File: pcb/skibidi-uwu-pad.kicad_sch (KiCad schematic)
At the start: 21 parts, among them J1 Conn_01x02_Socket, SW2 RotaryEncoder_Switch, SW3 SW_Push, SW4 SW_Push, SW5 PTS526 SM15 SMTR2 LFS, U1 XIAO-nRF52840-SMD, U2 AH49FNTR-G1, U3 AH49FNTR-G1, U4 AH49FNTR-G1

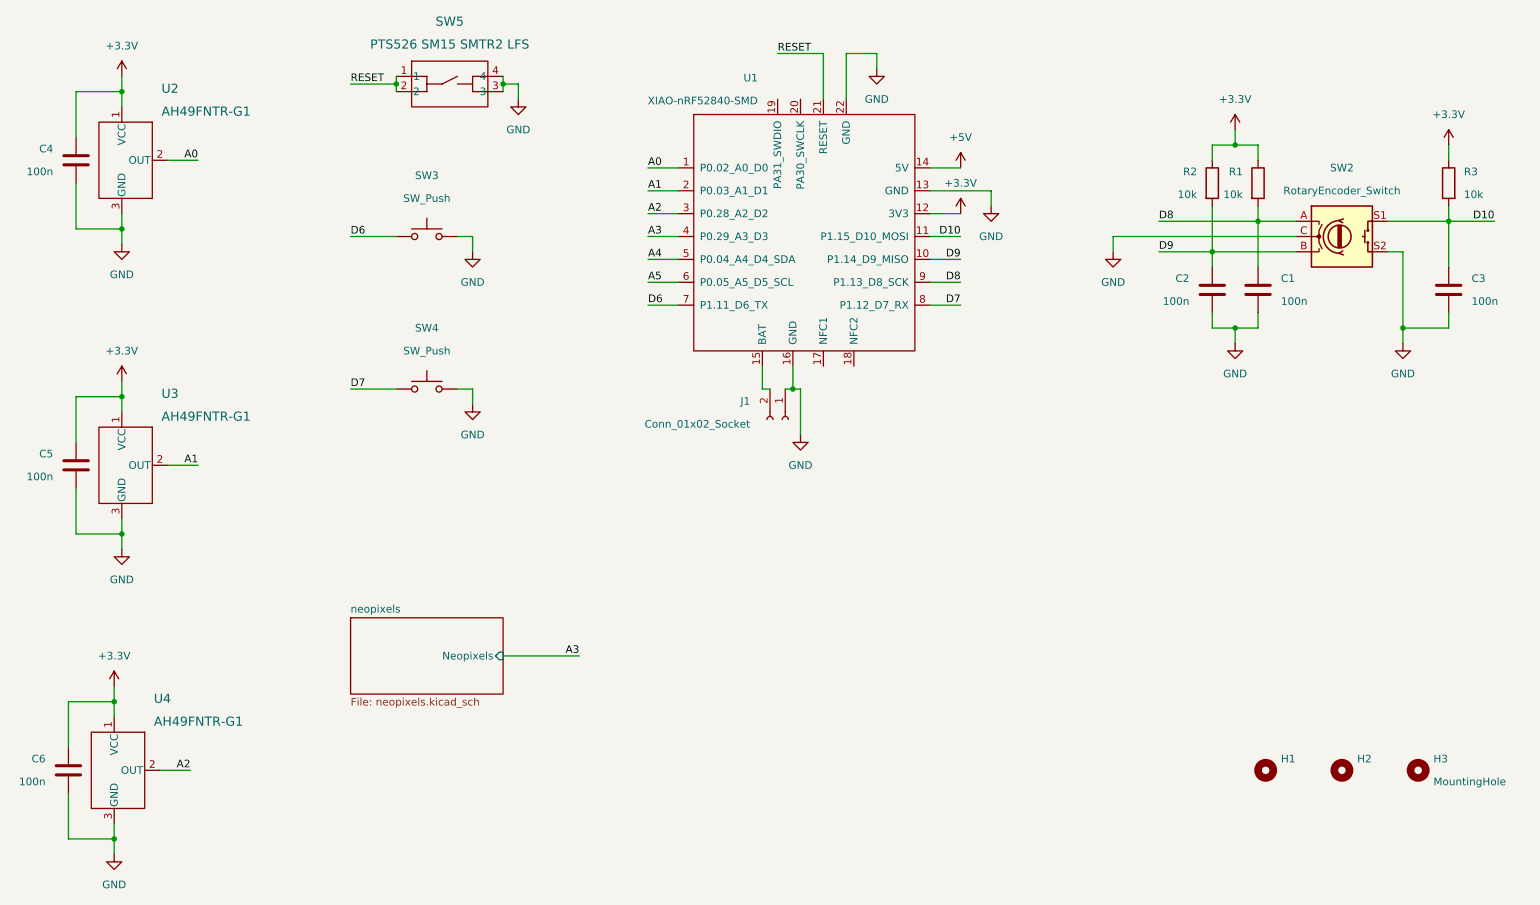
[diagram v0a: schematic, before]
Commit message: add smart power saving circuit + update readme
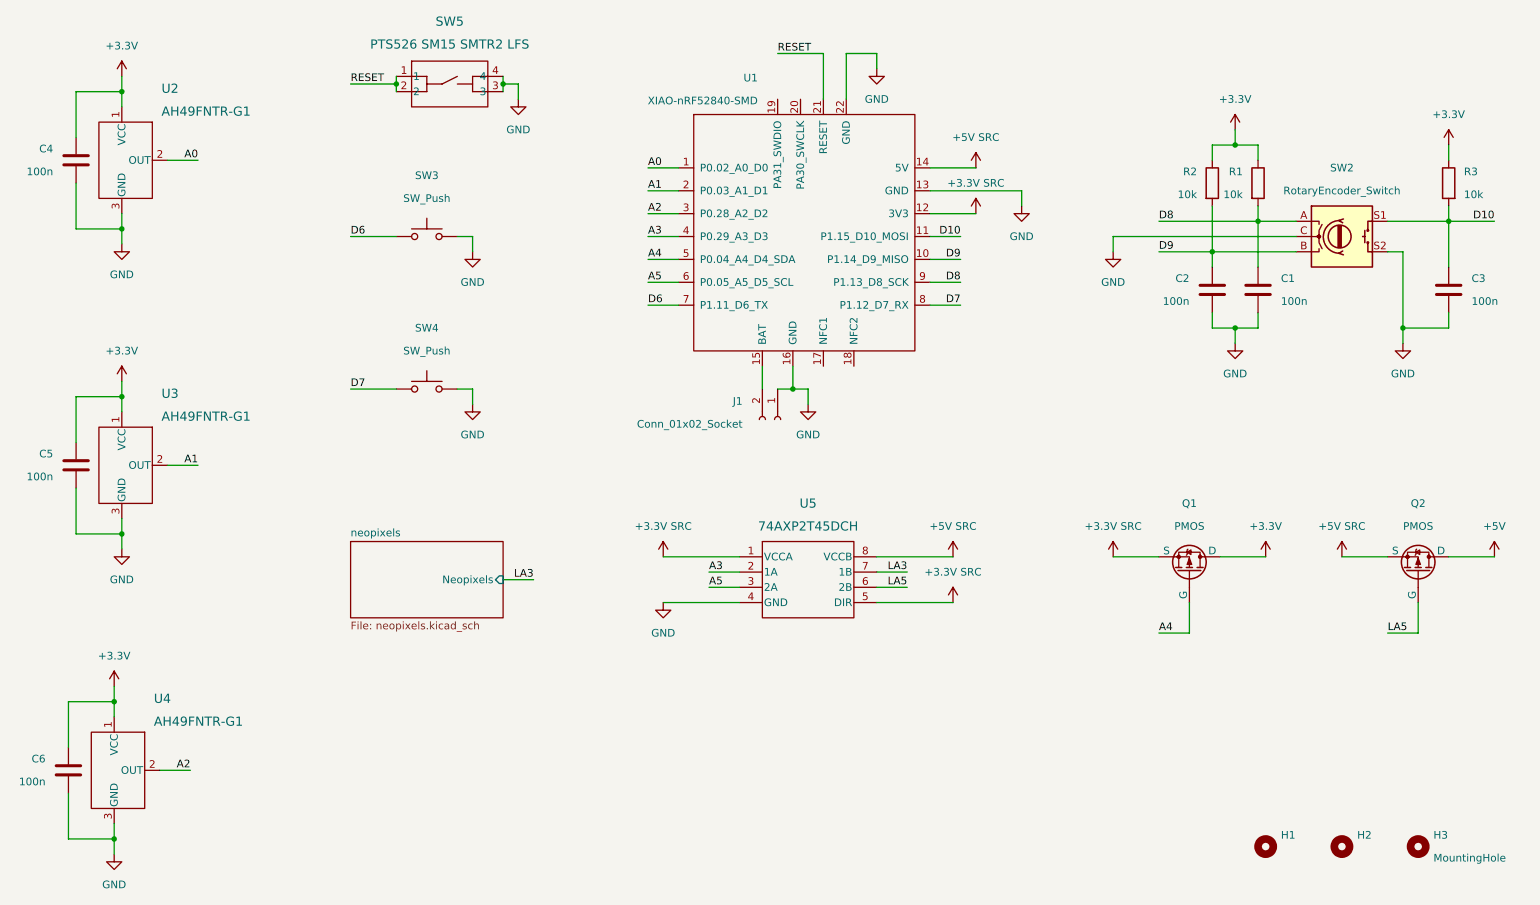
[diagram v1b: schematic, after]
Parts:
- added Q1, Q2: PMOS, Package_TO_SOT_SMD:SOT-23, symbol Simulation_SPICE:PMOS
- added U5: 74AXP2T45DCH, 74AXP2T45DCH:VSSOP8_SOT765-1_NEX, symbol 74AXP2T45DCH:74AXP2T45DCH
- SW5: footprint SON4_PTS526 SM15 SMTR2 LFS_CNK -> PTS526_SM15_SMTR2_LFS:SON4_PTS526 SM15 SMTR2 LFS_CNK
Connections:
- net +3.3V: now also Q1.1 (D); no longer U1.12 (3V3)
- net +5V: now also Q2.1 (D); no longer U1.14 (5V)
- net A3: now also U5.2 (1A)
- net A4: now also Q1.2 (G)
- net A5: now also U5.3 (2A)
- net GND: now also U5.4 (GND)
- new net +3.3V SRC: Q1.3 (S), U1.12 (3V3), U5.1 (VCCA), U5.5 (DIR)
- new net +5V SRC: Q2.3 (S), U1.14 (5V), U5.8 (VCCB)
- new net LA3: U5.7 (1B)
- new net LA5: Q2.2 (G), U5.6 (2B)
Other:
- moved on the sheet: H1, H2, H3, J1

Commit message: add schematic
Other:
- company: (none) -> Toby Cm's Lab
- title: (none) -> skibidi-uwu-pad
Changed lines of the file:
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@@
 	(generator_version "9.0")
 	(paper "A4")
+	(title_block
+		(title "skibidi-uwu-pad")
+		(date "2025-12-14")
+		(rev "v3")
+		(company "Toby Cm's Lab")
+	)
 	(junction
 		(at 50.8 100.33)
